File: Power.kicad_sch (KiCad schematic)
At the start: 25 parts, among them U201 AP62200WU-7, U202 TLV75733PDRV

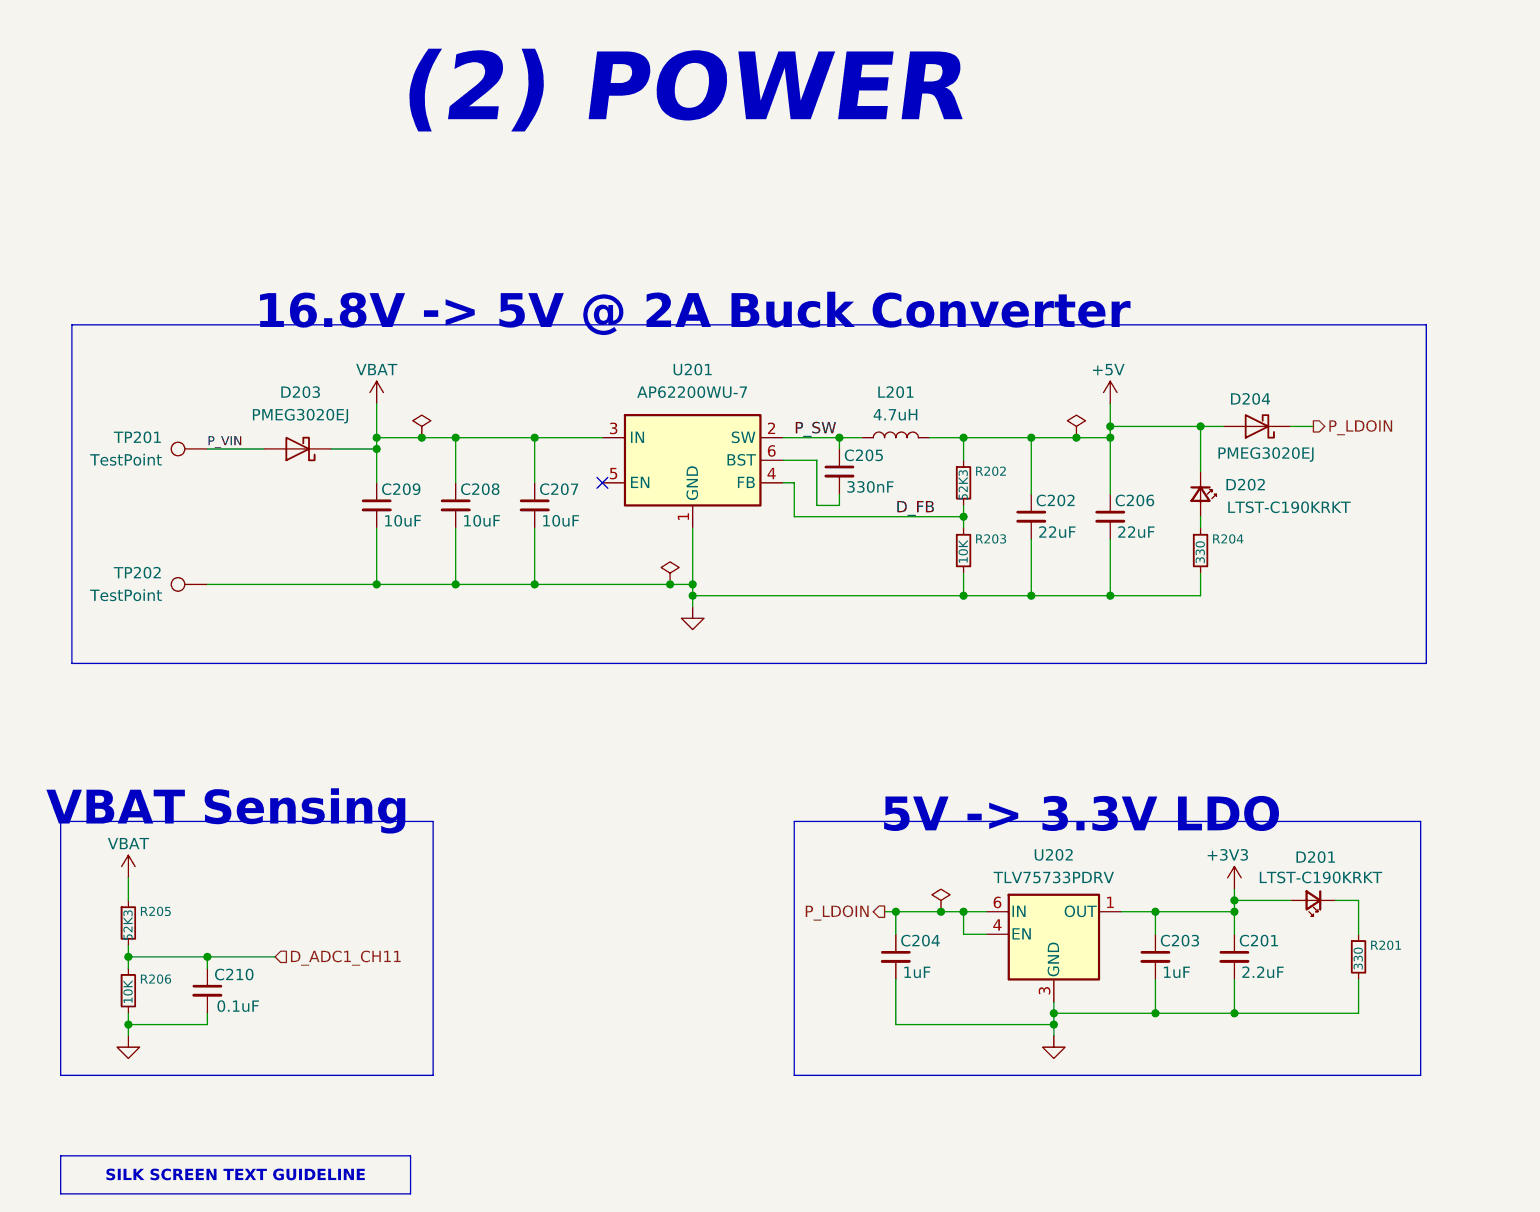
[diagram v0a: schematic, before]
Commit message: feat: add layout notes and net labels
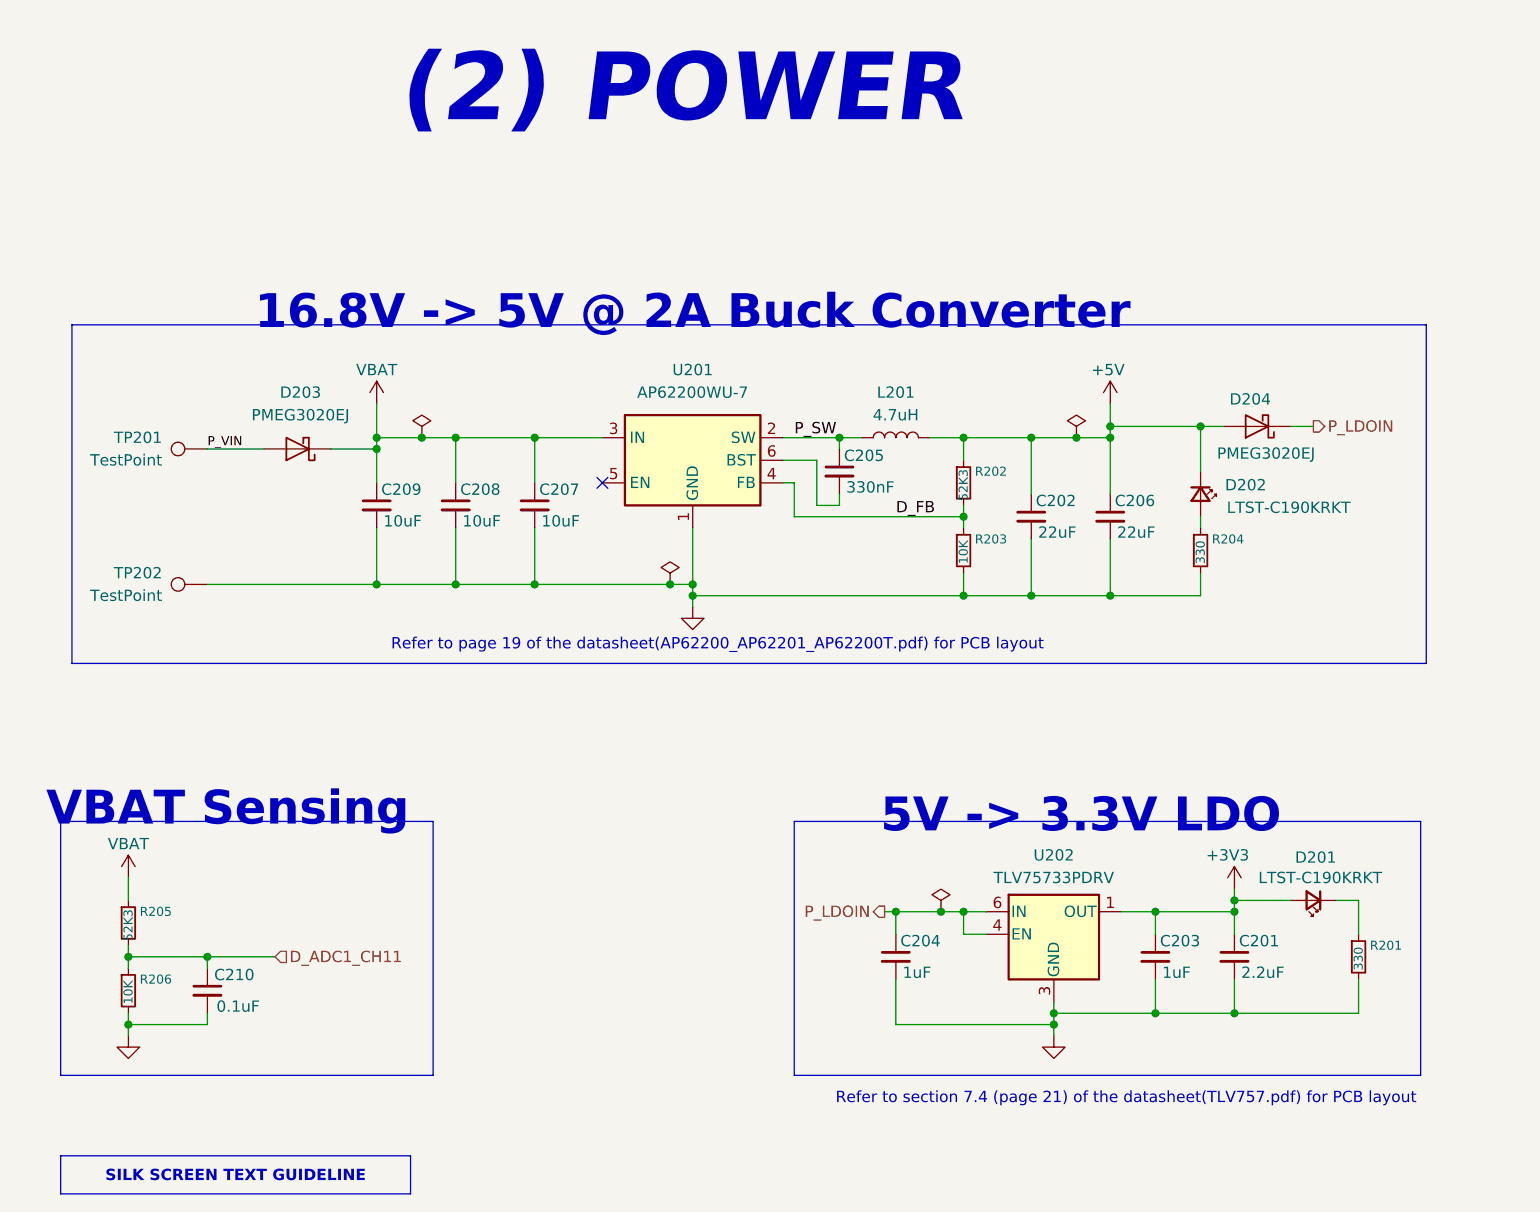
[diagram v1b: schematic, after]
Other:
- note added: "Refer to page 19 of the datasheet(AP62200_AP62201_AP62200T.pdf) for PCB layout"
- note added: "Refer to section 7.4 (page 21) of the datasheet(TLV757.pdf) for PCB layout"
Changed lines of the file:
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@@
+		)
+	)
+	(text "Refer to page 19 of the datasheet(AP62200_AP62201_AP62200T.pdf) for PCB layout"
+		(exclude_from_sim no)
+		(at 150.114 91.948 0)
+		(effects
+			(font
+				(size 1.27 1.27)
+			)
 		)
 	)
@@
 			)
 		)
+	)
+	(text "Refer to section 7.4 (page 21) of the datasheet(TLV757.pdf) for PCB layout"
+		(exclude_from_sim no)
+		(at 196.088 143.002 0)
+		(effects
+			(font
+				(size 1.27 1.27)
+			)
+		)

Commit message: refactor: change name from FeroFly405 to FeroFlyF405
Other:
- title: FeroFly405 -> FeroFlyF405
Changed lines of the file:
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@@
 	(paper "A4")
 	(title_block
-		(title "FeroFly405")
+		(title "FeroFlyF405")
 		(date "2026-07-22")
 		(rev "1")
-		(comment 3 "GitHub: https://github.com/Ozonised/FeroFly405")
+		(comment 3 "GitHub: https://github.com/Ozonised/FeroFlyF405")
 		(comment 4 "Designed by: Farhan Khan")
 	)
@@
 		)
 		(instances
-			(project "FeroFly"
+			(project "FeroFlyF405"
 				(path "/8fea5468-8d8d-4bdb-afc0-e65b62c92669/8c352998-3abb-4e27-b22f-570d9eb08340"
 					(reference "U201")
@@
 		)
 		(instances
-			(project "FeroFly"
+			(project "FeroFlyF405"
 				(path "/8fea5468-8d8d-4bdb-afc0-e65b62c92669/8c352998-3abb-4e27-b22f-570d9eb08340"
 					(reference "C209")
@@
 		)
 		(instances
-			(project "FeroFly"
+			(project "FeroFlyF405"
 				(path "/8fea5468-8d8d-4bdb-afc0-e65b62c92669/8c352998-3abb-4e27-b22f-570d9eb08340"
 					(reference "D204")
@@
 		)
 		(instances
-			(project "FeroFly"
+			(project "FeroFlyF405"
 				(path "/8fea5468-8d8d-4bdb-afc0-e65b62c92669/8c352998-3abb-4e27-b22f-570d9eb08340"
 					(reference "C208")
@@
 		)
 		(instances
-			(project "FeroFly"
+			(project "FeroFlyF405"
 				(path "/8fea5468-8d8d-4bdb-afc0-e65b62c92669/8c352998-3abb-4e27-b22f-570d9eb08340"
 					(reference "C201")
@@
 		)
 		(instances
-			(project "FeroFly"
+			(project "FeroFlyF405"
 				(path "/8fea5468-8d8d-4bdb-afc0-e65b62c92669/8c352998-3abb-4e27-b22f-570d9eb08340"
 					(reference "#PWR0202")
@@
 		)
 		(instances
-			(project "FeroFly"
+			(project "FeroFlyF405"
 				(path "/8fea5468-8d8d-4bdb-afc0-e65b62c92669/8c352998-3abb-4e27-b22f-570d9eb08340"
 					(reference "C204")
@@
 		)
 		(instances
-			(project "FeroFly"
+			(project "FeroFlyF405"
 				(path "/8fea5468-8d8d-4bdb-afc0-e65b62c92669/8c352998-3abb-4e27-b22f-570d9eb08340"
 					(reference "R204")
@@
 		)
 		(instances
-			(project "FeroFly"
+			(project "FeroFlyF405"
 				(path "/8fea5468-8d8d-4bdb-afc0-e65b62c92669/8c352998-3abb-4e27-b22f-570d9eb08340"
 					(reference "#FLG0204")
@@
 		)
 		(instances
-			(project "FeroFly"
+			(project "FeroFlyF405"
 				(path "/8fea5468-8d8d-4bdb-afc0-e65b62c92669/8c352998-3abb-4e27-b22f-570d9eb08340"
 					(reference "U202")
@@
 		)
 		(instances
-			(project "FeroFly"
+			(project "FeroFlyF405"
 				(path "/8fea5468-8d8d-4bdb-afc0-e65b62c92669/8c352998-3abb-4e27-b22f-570d9eb08340"
 					(reference "D203")
@@
 		)
 		(instances
-			(project "FeroFly"
+			(project "FeroFlyF405"
 				(path "/8fea5468-8d8d-4bdb-afc0-e65b62c92669/8c352998-3abb-4e27-b22f-570d9eb08340"
 					(reference "R206")
@@
 		)
 		(instances
-			(project "FeroFly"
+			(project "FeroFlyF405"
 				(path "/8fea5468-8d8d-4bdb-afc0-e65b62c92669/8c352998-3abb-4e27-b22f-570d9eb08340"
 					(reference "C210")
@@
 		)
 		(instances
-			(project "FeroFly"
+			(project "FeroFlyF405"
 				(path "/8fea5468-8d8d-4bdb-afc0-e65b62c92669/8c352998-3abb-4e27-b22f-570d9eb08340"
 					(reference "#PWR0206")
@@
 		)
 		(instances
-			(project "FeroFly"
+			(project "FeroFlyF405"
 				(path "/8fea5468-8d8d-4bdb-afc0-e65b62c92669/8c352998-3abb-4e27-b22f-570d9eb08340"
 					(reference "D202")
@@
 		)
 		(instances
-			(project "FeroFly"
+			(project "FeroFlyF405"
 				(path "/8fea5468-8d8d-4bdb-afc0-e65b62c92669/8c352998-3abb-4e27-b22f-570d9eb08340"
 					(reference "R201")
@@
 		)
 		(instances
-			(project "FeroFly"
+			(project "FeroFlyF405"
 				(path "/8fea5468-8d8d-4bdb-afc0-e65b62c92669/8c352998-3abb-4e27-b22f-570d9eb08340"
 					(reference "#PWR0203")
@@
 		)
 		(instances
-			(project "FeroFly"
+			(project "FeroFlyF405"
 				(path "/8fea5468-8d8d-4bdb-afc0-e65b62c92669/8c352998-3abb-4e27-b22f-570d9eb08340"
 					(reference "C207")
@@
 		)
 		(instances
-			(project "FeroFly"
+			(project "FeroFlyF405"
 				(path "/8fea5468-8d8d-4bdb-afc0-e65b62c92669/8c352998-3abb-4e27-b22f-570d9eb08340"
 					(reference "C202")
@@
 		)
 		(instances
-			(project "FeroFly"
+			(project "FeroFlyF405"
 				(path "/8fea5468-8d8d-4bdb-afc0-e65b62c92669/8c352998-3abb-4e27-b22f-570d9eb08340"
 					(reference "#PWR0214")
@@
 		)
 		(instances
-			(project "FeroFly"
+			(project "FeroFlyF405"
 				(path "/8fea5468-8d8d-4bdb-afc0-e65b62c92669/8c352998-3abb-4e27-b22f-570d9eb08340"
 					(reference "TP202")
@@
 		)
 		(instances
-			(project "FeroFly"
+			(project "FeroFlyF405"
 				(path "/8fea5468-8d8d-4bdb-afc0-e65b62c92669/8c352998-3abb-4e27-b22f-570d9eb08340"
 					(reference "R202")
@@
 		)
 		(instances
-			(project "FeroFly"
+			(project "FeroFlyF405"
 				(path "/8fea5468-8d8d-4bdb-afc0-e65b62c92669/8c352998-3abb-4e27-b22f-570d9eb08340"
 					(reference "C203")
@@
 		)
 		(instances
-			(project "FeroFly"
+			(project "FeroFlyF405"
 				(path "/8fea5468-8d8d-4bdb-afc0-e65b62c92669/8c352998-3abb-4e27-b22f-570d9eb08340"
 					(reference "TP201")
@@
 		)
 		(instances
-			(project "FeroFly"
+			(project "FeroFlyF405"
 				(path "/8fea5468-8d8d-4bdb-afc0-e65b62c92669/8c352998-3abb-4e27-b22f-570d9eb08340"
 					(reference "#FLG0203")
@@
 		)
 		(instances
-			(project "FeroFly"
+			(project "FeroFlyF405"
 				(path "/8fea5468-8d8d-4bdb-afc0-e65b62c92669/8c352998-3abb-4e27-b22f-570d9eb08340"
 					(reference "#FLG0202")
@@
 		)
 		(instances
-			(project "FeroFly"
+			(project "FeroFlyF405"
 				(path "/8fea5468-8d8d-4bdb-afc0-e65b62c92669/8c352998-3abb-4e27-b22f-570d9eb08340"
 					(reference "R205")
@@
 		)
 		(instances
-			(project "FeroFly"
+			(project "FeroFlyF405"
 				(path "/8fea5468-8d8d-4bdb-afc0-e65b62c92669/8c352998-3abb-4e27-b22f-570d9eb08340"
 					(reference "L201")
@@
 		)
 		(instances
-			(project "FeroFly"
+			(project "FeroFlyF405"
 				(path "/8fea5468-8d8d-4bdb-afc0-e65b62c92669/8c352998-3abb-4e27-b22f-570d9eb08340"
 					(reference "#FLG0201")
@@
 		)
 		(instances
-			(project "FeroFly"
+			(project "FeroFlyF405"
 				(path "/8fea5468-8d8d-4bdb-afc0-e65b62c92669/8c352998-3abb-4e27-b22f-570d9eb08340"
 					(reference "#PWR0204")
@@
 		)
 		(instances
-			(project "FeroFly"
+			(project "FeroFlyF405"
 				(path "/8fea5468-8d8d-4bdb-afc0-e65b62c92669/8c352998-3abb-4e27-b22f-570d9eb08340"
 					(reference "D201")
@@
 		)
 		(instances
-			(project "FeroFly"
+			(project "FeroFlyF405"
 				(path "/8fea5468-8d8d-4bdb-afc0-e65b62c92669/8c352998-3abb-4e27-b22f-570d9eb08340"
 					(reference "R203")
@@
 		)
 		(instances
-			(project "FeroFly"
+			(project "FeroFlyF405"
 				(path "/8fea5468-8d8d-4bdb-afc0-e65b62c92669/8c352998-3abb-4e27-b22f-570d9eb08340"
 					(reference "#PWR0215")
@@
 		)
 		(instances
-			(project "FeroFly"
+			(project "FeroFlyF405"
 				(path "/8fea5468-8d8d-4bdb-afc0-e65b62c92669/8c352998-3abb-4e27-b22f-570d9eb08340"
 					(reference "C206")
@@
 		)
 		(instances
-			(project "FeroFly"
+			(project "FeroFlyF405"
 				(path "/8fea5468-8d8d-4bdb-afc0-e65b62c92669/8c352998-3abb-4e27-b22f-570d9eb08340"
 					(reference "C205")
@@
 		)
 		(instances
-			(project "FeroFly"
+			(project "FeroFlyF405"
 				(path "/8fea5468-8d8d-4bdb-afc0-e65b62c92669/8c352998-3abb-4e27-b22f-570d9eb08340"
 					(reference "#PWR0205")

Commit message: fix: change footprint for IO & LDO
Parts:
- U202: footprint Package_SON:WSON-6-1EP_2x2mm_P0.65mm_EP1x1.6mm_ThermalVias -> Package_SON:WSON-6-1EP_2x2mm_P0.65mm_EP1x1.6mm
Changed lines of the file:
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@@
 			)
 		)
-		(property "Footprint" "Package_SON:WSON-6-1EP_2x2mm_P0.65mm_EP1x1.6mm_ThermalVias"
+		(property "Footprint" "Package_SON:WSON-6-1EP_2x2mm_P0.65mm_EP1x1.6mm"
 			(at 187.96 116.205 0)
 			(hide yes)
